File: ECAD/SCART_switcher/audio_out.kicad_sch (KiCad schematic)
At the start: 31 parts, among them U34 RC4580, U35 RC4580, U36 RC4580

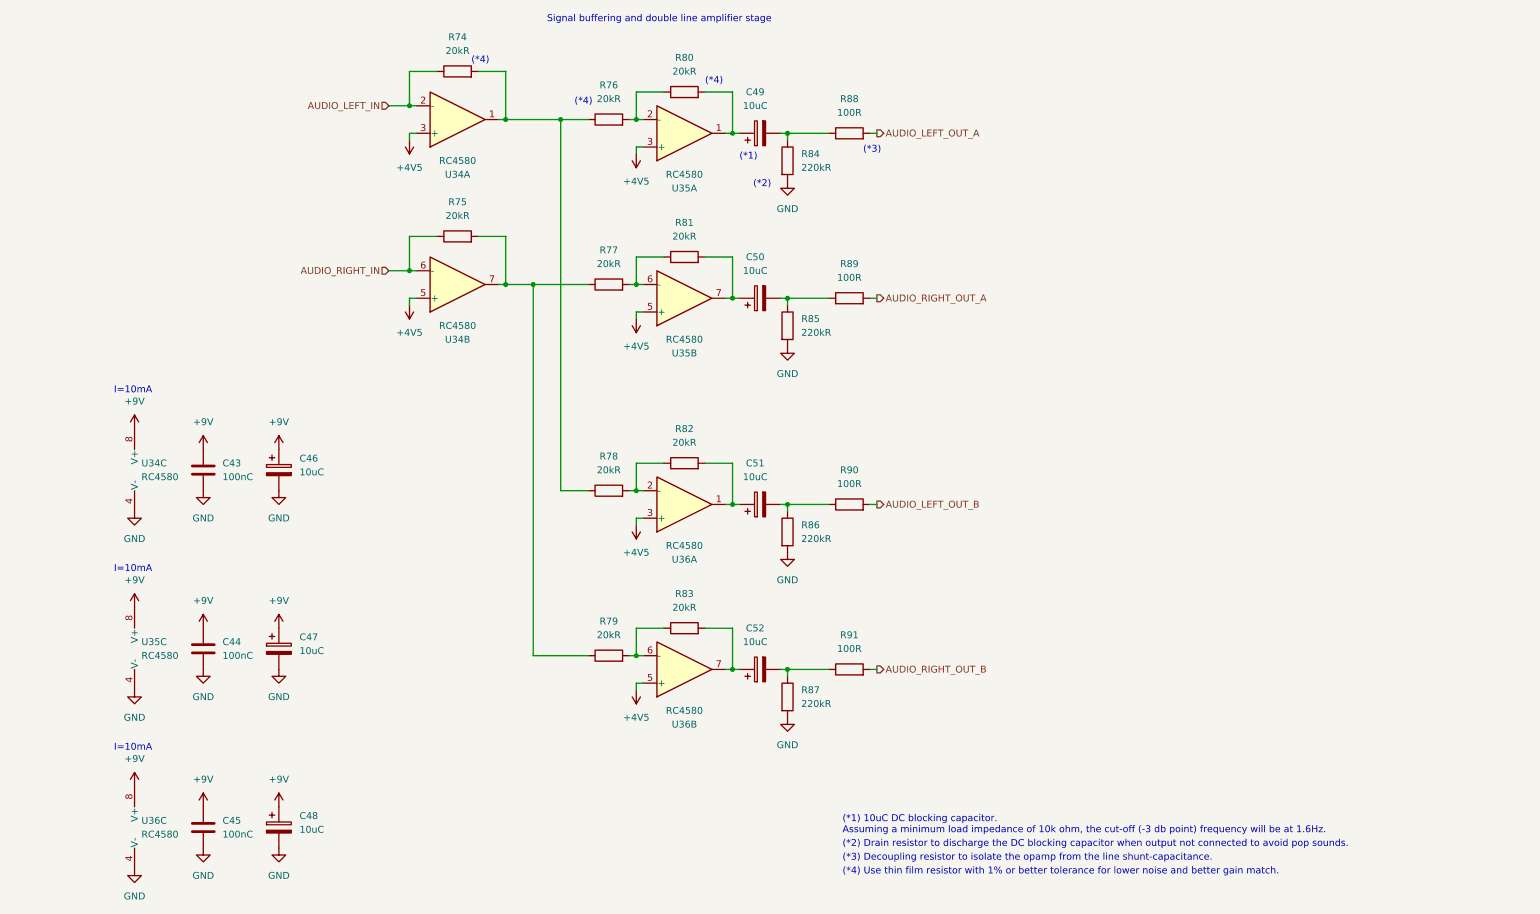
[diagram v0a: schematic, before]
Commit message: Cleanup and new power supply pcb
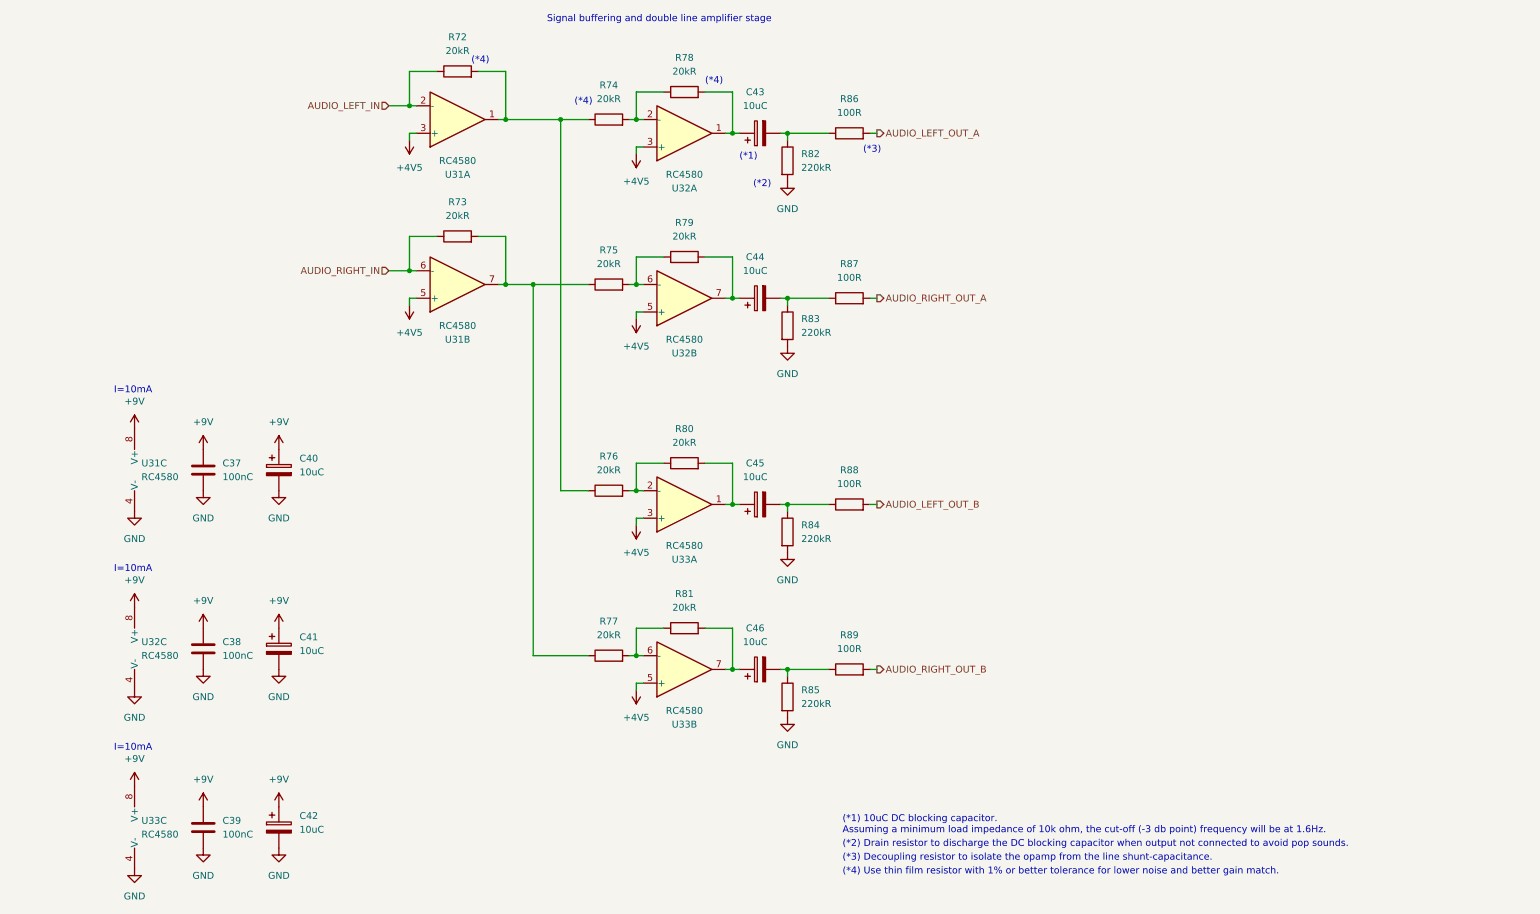
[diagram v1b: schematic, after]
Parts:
- renumbered C43 to C37, C44 to C38, C45 to C39, C46 to C40, C47 to C41, C48 to C42, C49 to C43, C50 to C44, C51 to C45, C52 to C46, R74 to R72, R75 to R73, R76 to R74, R77 to R75, R78 to R76, R79 to R77, R80 to R78, R81 to R79, R82 to R80, R83 to R81, R84 to R82, R85 to R83, R86 to R84, R87 to R85, R88 to R86, R89 to R87, R90 to R88, R91 to R89, U34 to U31, U35 to U32, U36 to U33

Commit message: Progressed ECAD.
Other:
- note added: "RC4580 can be replaced with higher quality OPA1656."
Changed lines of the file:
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@@
+    (effects (font (size 1.27 1.27)) (justify left bottom))
+  )
+  (text "RC4580 can be replaced with higher quality OPA1656."
+    (at 24.13 52.07 0)
     (effects (font (size 1.27 1.27)) (justify left bottom))
   )

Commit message: Progressed ECAD.
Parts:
- renumbered C37 to C35, C38 to C36, C39 to C37, C40 to C38, C41 to C39, C42 to C40, C43 to C41, C44 to C42, C45 to C43, C46 to C44

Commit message: Progressed ECAD.
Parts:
- renumbered R72 to R74, R73 to R75, R74 to R76, R75 to R77, R76 to R78, R77 to R79, R78 to R80, R79 to R81, R80 to R82, R81 to R83, R82 to R84, R83 to R85, R84 to R86, R85 to R87, R86 to R88, R87 to R89, R88 to R90, R89 to R91

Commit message: Progressed ECAD.
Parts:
- C35, C36, C37: MPN CL21B104KBCNNNC -> CL10B104KO8NNNC; Status (none) -> OK
- R74, R75, R76, R77, R78, R79, R80, R81, R82, R83: MPN (none) -> RT0805BRC0720KL; Status (none) -> OK
- R84, R85, R86, R87: MPN (none) -> RT0805DRD07220KL; Status (none) -> OK
- R88, R89, R90, R91: MPN (none) -> RT0805BRD07100RL; Status (none) -> OK

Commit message: Progressed ECAD.
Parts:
- U31, U32, U33: MPN RC4580IDR -> OPA1656ID; MPN_MOUSER (none) -> OPA1656ID

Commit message: Progressed ECAD.
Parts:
- U31, U32, U33: value RC4580 -> OPA1656; MPN OPA1656ID -> OPA1656IDR; MPN_MOUSER OPA1656ID -> OPA1656IDR
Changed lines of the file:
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@@
       (effects (font (size 1.27 1.27)) (justify left))
     )
-    (property "Value" "RC4580" (at 48.26 138.43 0)
+    (property "Value" "OPA1656" (at 48.26 138.43 0)
       (effects (font (size 1.27 1.27)) (justify left))
     )
@@
       (effects (font (size 1.27 1.27)) hide)
     )
-    (property "Datasheet" "https://datasheet.lcsc.com/lcsc/2304140030_Texas-Instruments-RC4580IDR_C80100.pdf" (at 49.53 137.16 0)
-      (effects (font (size 1.27 1.27)) hide)
-    )
-    (property "MPN" "OPA1656ID" (at 49.53 137.16 0)
+    (property "Datasheet" "https://datasheet.lcsc.com/lcsc/2303020130_Texas-Instruments-OPA1656IDR_C1849431.pdf" (at 49.53 137.16 0)
+      (effects (font (size 1.27 1.27)) hide)
+    )
+    (property "MPN" "OPA1656IDR" (at 49.53 137.16 0)
       (effects (font (size 1.27 1.27)) hide)
     )
@@
       (effects (font (size 1.27 1.27)) hide)
     )
-    (property "MPN_MOUSER" "OPA1656ID" (at 49.53 137.16 0)
+    (property "MPN_MOUSER" "OPA1656IDR" (at 49.53 137.16 0)
       (effects (font (size 1.27 1.27)) hide)
     )
@@
       (effects (font (size 1.27 1.27)) (justify left))
     )
-    (property "Value" "RC4580" (at 48.26 105.41 0)
+    (property "Value" "OPA1656" (at 48.26 105.41 0)
       (effects (font (size 1.27 1.27)) (justify left))
     )
@@
       (effects (font (size 1.27 1.27)) hide)
     )
-    (property "Datasheet" "https://datasheet.lcsc.com/lcsc/2304140030_Texas-Instruments-RC4580IDR_C80100.pdf" (at 49.53 104.14 0)
-      (effects (font (size 1.27 1.27)) hide)
-    )
-    (property "MPN" "OPA1656ID" (at 49.53 104.14 0)
+    (property "Datasheet" "https://datasheet.lcsc.com/lcsc/2303020130_Texas-Instruments-OPA1656IDR_C1849431.pdf" (at 49.53 104.14 0)
+      (effects (font (size 1.27 1.27)) hide)
+    )
+    (property "MPN" "OPA1656IDR" (at 49.53 104.14 0)
       (effects (font (size 1.27 1.27)) hide)
     )
@@
       (effects (font (size 1.27 1.27)) hide)
     )
-    (property "MPN_MOUSER" "OPA1656ID" (at 49.53 104.14 0)
+    (property "MPN_MOUSER" "OPA1656IDR" (at 49.53 104.14 0)
       (effects (font (size 1.27 1.27)) hide)
     )
@@
       (effects (font (size 1.27 1.27)))
     )
-    (property "Value" "RC4580" (at 106.68 46.99 0)
+    (property "Value" "OPA1656" (at 106.68 46.99 0)
       (effects (font (size 1.27 1.27)))
     )
@@
       (effects (font (size 1.27 1.27)) hide)
     )
-    (property "Datasheet" "https://datasheet.lcsc.com/lcsc/2304140030_Texas-Instruments-RC4580IDR_C80100.pdf" (at 106.68 39.37 0)
-      (effects (font (size 1.27 1.27)) hide)
-    )
-    (property "MPN" "OPA1656ID" (at 106.68 39.37 0)
+    (property "Datasheet" "https://datasheet.lcsc.com/lcsc/2303020130_Texas-Instruments-OPA1656IDR_C1849431.pdf" (at 106.68 39.37 0)
+      (effects (font (size 1.27 1.27)) hide)
+    )
+    (property "MPN" "OPA1656IDR" (at 106.68 39.37 0)
       (effects (font (size 1.27 1.27)) hide)
     )
@@
       (effects (font (size 1.27 1.27)) hide)
     )
-    (property "MPN_MOUSER" "OPA1656ID" (at 106.68 39.37 0)
+    (property "MPN_MOUSER" "OPA1656IDR" (at 106.68 39.37 0)
       (effects (font (size 1.27 1.27)) hide)
     )
@@
       (effects (font (size 1.27 1.27)))
     )
-    (property "Value" "RC4580" (at 148.59 148.59 0)
+    (property "Value" "OPA1656" (at 148.59 148.59 0)
       (effects (font (size 1.27 1.27)))
     )
@@
       (effects (font (size 1.27 1.27)) hide)
     )
-    (property "Datasheet" "https://datasheet.lcsc.com/lcsc/2304140030_Texas-Instruments-RC4580IDR_C80100.pdf" (at 148.59 140.97 0)
-      (effects (font (size 1.27 1.27)) hide)
-    )
-    (property "MPN" "OPA1656ID" (at 148.59 140.97 0)
+    (property "Datasheet" "https://datasheet.lcsc.com/lcsc/2303020130_Texas-Instruments-OPA1656IDR_C1849431.pdf" (at 148.59 140.97 0)
+      (effects (font (size 1.27 1.27)) hide)
+    )
+    (property "MPN" "OPA1656IDR" (at 148.59 140.97 0)
       (effects (font (size 1.27 1.27)) hide)
     )
@@
       (effects (font (size 1.27 1.27)) hide)
     )
-    (property "MPN_MOUSER" "OPA1656ID" (at 148.59 140.97 0)
+    (property "MPN_MOUSER" "OPA1656IDR" (at 148.59 140.97 0)
       (effects (font (size 1.27 1.27)) hide)
     )
@@
       (effects (font (size 1.27 1.27)))
     )
-    (property "Value" "RC4580" (at 148.59 80.01 0)
+    (property "Value" "OPA1656" (at 148.59 80.01 0)
       (effects (font (size 1.27 1.27)))
     )
@@
       (effects (font (size 1.27 1.27)) hide)
     )
-    (property "Datasheet" "https://datasheet.lcsc.com/lcsc/2304140030_Texas-Instruments-RC4580IDR_C80100.pdf" (at 148.59 72.39 0)
-      (effects (font (size 1.27 1.27)) hide)
-    )
-    (property "MPN" "OPA1656ID" (at 148.59 72.39 0)
+    (property "Datasheet" "https://datasheet.lcsc.com/lcsc/2303020130_Texas-Instruments-OPA1656IDR_C1849431.pdf" (at 148.59 72.39 0)
+      (effects (font (size 1.27 1.27)) hide)
+    )
+    (property "MPN" "OPA1656IDR" (at 148.59 72.39 0)
       (effects (font (size 1.27 1.27)) hide)
     )
@@
       (effects (font (size 1.27 1.27)) hide)
     )
-    (property "MPN_MOUSER" "OPA1656ID" (at 148.59 72.39 0)
+    (property "MPN_MOUSER" "OPA1656IDR" (at 148.59 72.39 0)
       (effects (font (size 1.27 1.27)) hide)
     )
@@
       (effects (font (size 1.27 1.27)))
     )
-    (property "Value" "RC4580" (at 148.59 118.11 0)
+    (property "Value" "OPA1656" (at 148.59 118.11 0)
       (effects (font (size 1.27 1.27)))
     )
@@
       (effects (font (size 1.27 1.27)) hide)
     )
-    (property "Datasheet" "https://datasheet.lcsc.com/lcsc/2304140030_Texas-Instruments-RC4580IDR_C80100.pdf" (at 148.59 110.49 0)
-      (effects (font (size 1.27 1.27)) hide)
-    )
-    (property "MPN" "OPA1656ID" (at 148.59 110.49 0)
+    (property "Datasheet" "https://datasheet.lcsc.com/lcsc/2303020130_Texas-Instruments-OPA1656IDR_C1849431.pdf" (at 148.59 110.49 0)
+      (effects (font (size 1.27 1.27)) hide)
+    )
+    (property "MPN" "OPA1656IDR" (at 148.59 110.49 0)
       (effects (font (size 1.27 1.27)) hide)
     )
@@
       (effects (font (size 1.27 1.27)) hide)
     )
-    (property "MPN_MOUSER" "OPA1656ID" (at 148.59 110.49 0)
+    (property "MPN_MOUSER" "OPA1656IDR" (at 148.59 110.49 0)
       (effects (font (size 1.27 1.27)) hide)
     )
@@
       (effects (font (size 1.27 1.27)) (justify left))
     )
-    (property "Value" "RC4580" (at 48.26 171.45 0)
+    (property "Value" "OPA1656" (at 48.26 171.45 0)
       (effects (font (size 1.27 1.27)) (justify left))
     )
@@
       (effects (font (size 1.27 1.27)) hide)
     )
-    (property "Datasheet" "https://datasheet.lcsc.com/lcsc/2304140030_Texas-Instruments-RC4580IDR_C80100.pdf" (at 49.53 170.18 0)
-      (effects (font (size 1.27 1.27)) hide)
-    )
-    (property "MPN" "OPA1656ID" (at 49.53 170.18 0)
+    (property "Datasheet" "https://datasheet.lcsc.com/lcsc/2303020130_Texas-Instruments-OPA1656IDR_C1849431.pdf" (at 49.53 170.18 0)
+      (effects (font (size 1.27 1.27)) hide)
+    )
+    (property "MPN" "OPA1656IDR" (at 49.53 170.18 0)
       (effects (font (size 1.27 1.27)) hide)
     )
@@
       (effects (font (size 1.27 1.27)) hide)
     )
-    (property "MPN_MOUSER" "OPA1656ID" (at 49.53 170.18 0)
+    (property "MPN_MOUSER" "OPA1656IDR" (at 49.53 170.18 0)
       (effects (font (size 1.27 1.27)) hide)
     )
@@
       (effects (font (size 1.27 1.27)))
     )
-    (property "Value" "RC4580" (at 106.68 77.47 0)
+    (property "Value" "OPA1656" (at 106.68 77.47 0)
       (effects (font (size 1.27 1.27)))
     )
@@
       (effects (font (size 1.27 1.27)) hide)
     )
-    (property "Datasheet" "https://datasheet.lcsc.com/lcsc/2304140030_Texas-Instruments-RC4580IDR_C80100.pdf" (at 106.68 69.85 0)
-      (effects (font (size 1.27 1.27)) hide)
-    )
-    (property "MPN" "OPA1656ID" (at 106.68 69.85 0)
+    (property "Datasheet" "https://datasheet.lcsc.com/lcsc/2303020130_Texas-Instruments-OPA1656IDR_C1849431.pdf" (at 106.68 69.85 0)
+      (effects (font (size 1.27 1.27)) hide)
+    )
+    (property "MPN" "OPA1656IDR" (at 106.68 69.85 0)
       (effects (font (size 1.27 1.27)) hide)
     )
@@
       (effects (font (size 1.27 1.27)) hide)
     )
-    (property "MPN_MOUSER" "OPA1656ID" (at 106.68 69.85 0)
+    (property "MPN_MOUSER" "OPA1656IDR" (at 106.68 69.85 0)
       (effects (font (size 1.27 1.27)) hide)
     )
@@
       (effects (font (size 1.27 1.27)))
     )
-    (property "Value" "RC4580" (at 148.59 49.53 0)
+    (property "Value" "OPA1656" (at 148.59 49.53 0)
       (effects (font (size 1.27 1.27)))
     )
@@
       (effects (font (size 1.27 1.27)) hide)
     )
-    (property "Datasheet" "https://datasheet.lcsc.com/lcsc/2304140030_Texas-Instruments-RC4580IDR_C80100.pdf" (at 148.59 41.91 0)
-      (effects (font (size 1.27 1.27)) hide)
-    )
-    (property "MPN" "OPA1656ID" (at 148.59 41.91 0)
+    (property "Datasheet" "https://datasheet.lcsc.com/lcsc/2303020130_Texas-Instruments-OPA1656IDR_C1849431.pdf" (at 148.59 41.91 0)
+      (effects (font (size 1.27 1.27)) hide)
+    )
+    (property "MPN" "OPA1656IDR" (at 148.59 41.91 0)
       (effects (font (size 1.27 1.27)) hide)
     )
@@
       (effects (font (size 1.27 1.27)) hide)
     )
-    (property "MPN_MOUSER" "OPA1656ID" (at 148.59 41.91 0)
-      (effects (font (size 1.27 1.27)) hide)
-    )
+    (property "MPN_MOUSER" "OPA1656IDR" (at 148.59 41.91 0)
+      (effects (font (size 1.27 1.27)) hide)
+    )

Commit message: Progressed ECAD.
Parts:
- R74, R75, R76, R77, R78, R79, R80, R81, R82, R83: MPN RT0805BRC0720KL -> RT0805FRE0720KL; R % tol (none) -> 1%; R pwr (none) -> 125mW
- R84, R85, R86, R87: MPN RT0805DRD07220KL -> RC0805JR-07220KL; R % tol (none) -> 5%; R pwr (none) -> 125mW
- R88, R89, R90, R91: MPN RT0805BRD07100RL -> RT0805FRD07100RL; R % tol (none) -> 1%; R pwr (none) -> 125mW
